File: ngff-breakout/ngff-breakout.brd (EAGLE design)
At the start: 90 x 80 mm, 77 parts, among them U2 LD1085D2T33R, X1 PINHD-2X4, X7 694108106102, X9 ZX360D-B-10P(30), Y4 MHF4, Y5 MHF4, Y6 MHF4

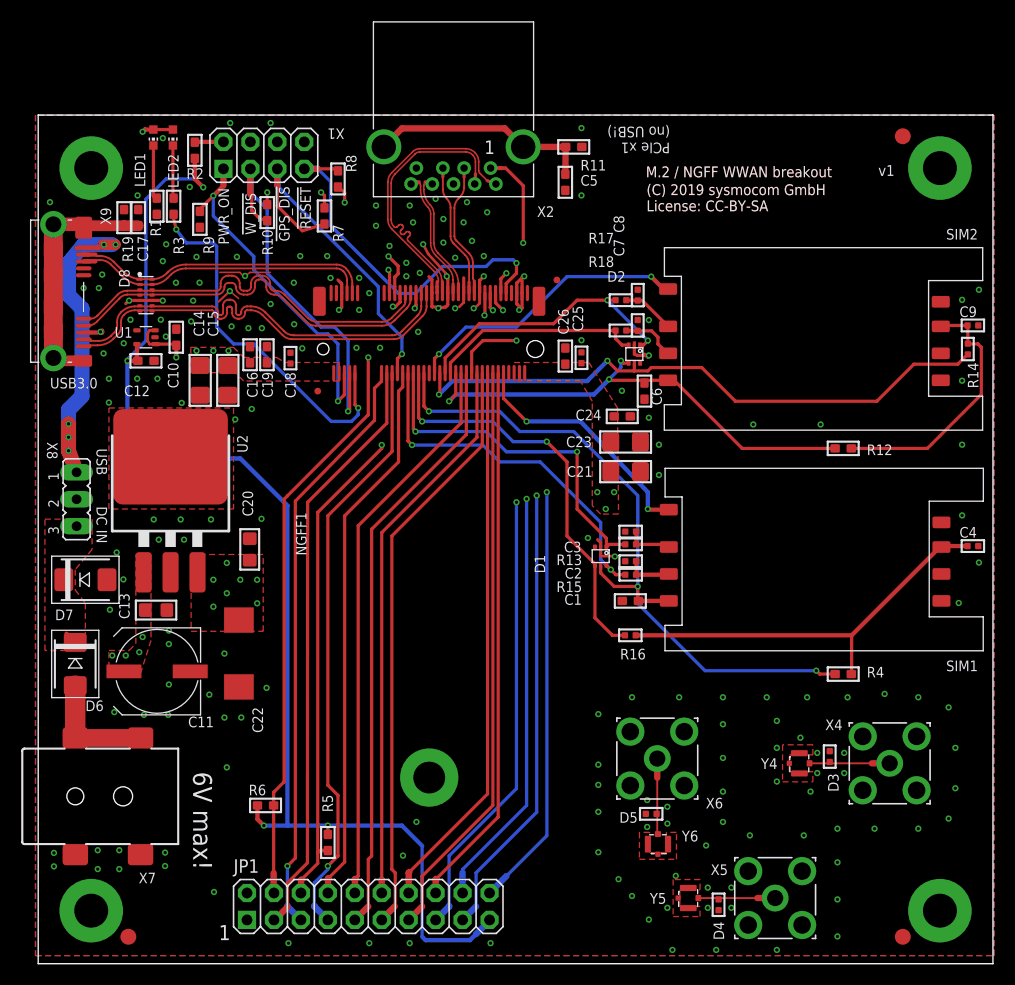
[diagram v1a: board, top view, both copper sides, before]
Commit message: ngff: move PCIe header 3mm inwards (solves OS#4210)
... and started OS#4211.
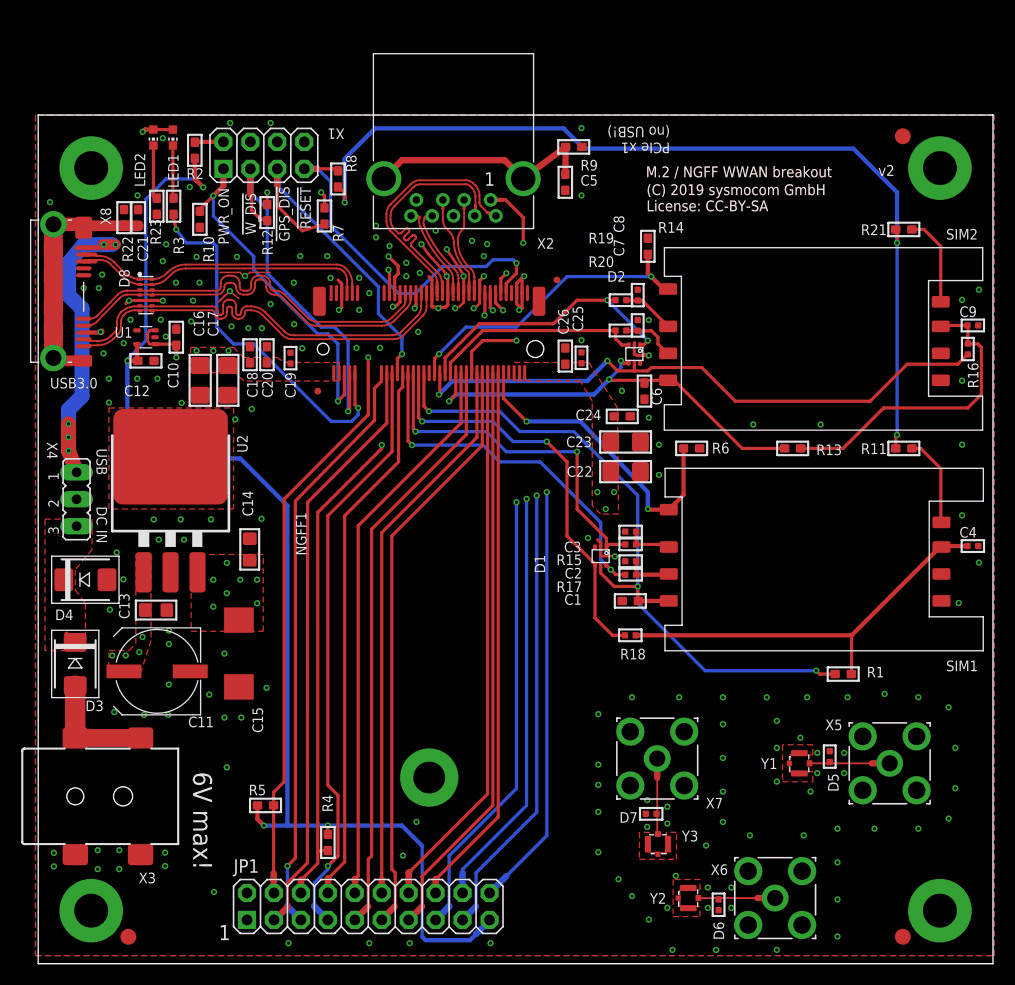
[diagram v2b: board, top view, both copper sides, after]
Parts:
- removed X9: ZX360D-B-10P(30), USB30-MICROB:ZX360D-B
- added R20: 47, rc-sysmocom:_0402
- added R21: 4.7k, rc-sysmocom:_0603
- added R22, R23: 330, rc-sysmocom:_0603
- added X3: 694108106102, Wurth_Elektronik_Electromechanic_DC_Power_Jack_Connectors_rev15c:694108106102
- C1, C10, C12, C24, C26, C5, C6: device rc-sysmocom:_0603 -> rc-sysmocom:_0603@1
- C13: device rc-sysmocom:_0805 -> rc-sysmocom:_0805@1
- C14: value 100u -> 10u; device rc-sysmocom:1206 -> rc-sysmocom:_0805@1
- C15: value 100u -> DNP; device rc-sysmocom:1206 -> rcl:SMC_E
- C16, C17: value 100n -> 100u; device rc-sysmocom:_0603 -> rc-sysmocom:1206@1
- C18: value 33p -> 100n; device rc-sysmocom:_0402 -> rc-sysmocom:_0603@1
- C19: value 10p -> 33p; device rc-sysmocom:_0603 -> rc-sysmocom:_0402@1
- C2, C25, C3, C4, C7, C8, C9: device rc-sysmocom:_0402 -> rc-sysmocom:_0402@1
- C20: value 10u -> 10p; device rc-sysmocom:_0805 -> rc-sysmocom:_0603@1
- C21: value 100u -> 100n; device rc-sysmocom:1206 -> rc-sysmocom:_0603@1
- C22: value DNP -> 100u; device rcl:SMC_E -> rc-sysmocom:1206@1
- C23: device rc-sysmocom:1206 -> rc-sysmocom:1206@1
- D3: value GG040205170N2P -> SD2114S040S5R0; device diodes-sysmocom:_0402 -> diodes-sysmocom:SMBDIODE
- D4: value GG040205170N2P -> SMBJP6KE6.8A-TP; device diodes-sysmocom:_0402 -> diodes-sysmocom:SMBDIODE
- D6: value SD2114S040S5R0 -> GG040205170N2P; device diodes-sysmocom:SMBDIODE -> diodes-sysmocom:_0402
- D7: value SMBJP6KE6.8A-TP -> GG040205170N2P; device diodes-sysmocom:SMBDIODE -> diodes-sysmocom:_0402
- LED1: value GREEN -> YELLOW
- LED2: value YELLOW -> GREEN
- R1: value 330 -> DNP
- R10: value 10k -> 100k
- R11: value 330 -> 4.7k
- R12, R4: value DNP -> 10k
- R13: value 47 -> DNP; device rc-sysmocom:_0402 -> rc-sysmocom:_0603
- R14: value 47 -> 47k; device rc-sysmocom:_0402 -> rc-sysmocom:_0603
- R19: value 330 -> 47; device rc-sysmocom:_0603 -> rc-sysmocom:_0402
- R6: value 10k -> 47k
- R9: value 100k -> 330
- X4: device laforge:SMA-F-S-TH -> jumper:JP2
- X7: value 694108106102 -> (none); device Wurth_Elektronik_Electromechanic_DC_Power_Jack_Connectors_rev15c:694108106102 -> laforge:SMA-F-S-TH
- X8: value (none) -> ZX360D-B-10P(30); device jumper:JP2 -> USB30-MICROB:ZX360D-B
- moved X4 80.6 mm to (3.62, 43.8), turned to 270 degrees
- moved R1 78.3 mm to (75.9, 27.3), turned to 0 degrees
- moved D3 71.7 mm to (3.49, 28.3)
- moved D4 67.1 mm to (4.45, 36.2), turned to 0 degrees
- moved D6 64.8 mm to (64.1, 5.56), turned to 90 degrees
- moved X7 60.0 mm to (58.4, 19.3), turned to 180 degrees
- moved R12 58.7 mm to (21.6, 70.8), turned to 90 degrees
- moved D7 57.7 mm to (57.8, 14.1)
- moved R6 52.4 mm to (61.6, 48.6)
- moved C21 51.8 mm to (9.43, 70.3), turned to 270 degrees
- moved R4 51.1 mm to (27.3, 11.4), turned to 90 degrees
- moved R19 47.5 mm to (54.9, 62.5), turned to 0 degrees
- moved R11 42.1 mm to (81.6, 48.6), turned to 0 degrees
- moved R16 41.7 mm to (87.6, 57.9), turned to 90 degrees
- moved C22 40.3 mm to (55.4, 46.4), turned to 180 degrees
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- renumbered JP501 to JP2, JP502 to JP3, Y4 to Y1, Y5 to Y2, Y6 to Y3
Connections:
- new net N$11: R21.2, SIM2.82
- new net N$9: R11.2, SIM1.82
- net !BODY_SAR: now also R5.1; no longer R6.1
- net !USIM1_RESET: now also R17.2; no longer R15.2
- net !USIM2_RESET: now also R20.2; no longer R18.2
- net !WAKE_ON_WWAN: now also R4.1; no longer R5.1
- net !W_DISABLE: now also R12.1; no longer R10.1
- net GND: now also C15.-, C18.1, C20.2, C22.1, D4.A, D6.1, D7.1, R10.1, R14.1, R22.1, R23.1, R6.1, X3.2, X3.3, X7.G1, X7.G2, X7.G3, X7.G4, X8.5, X8.8; no longer C15.1, C18.2, C20.1, C22.-, D3.1, D4.1, D7.A, R1.1, R11.1, R19.1, SIM1.82, SIM2.82, X4.G1, X4.G2, X4.G3, X4.G4, X7.2, X7.3, X9.5, X9.8
- net LDO_IN: now also X4.2; no longer X8.2
- net N$1: now also LED2.C, R23.2; no longer LED1.C, R1.2
- net N$10: now also C21.2, R22.2, X8.S1, X8.S2, X8.S3, X8.S4, X8.S5, X8.S6, X8.S7, X8.S8; no longer C17.2, R19.2, X9.S1, X9.S2, X9.S3, X9.S4, X9.S5, X9.S6, X9.S7, X9.S8
- net N$12: now also D3.C, D4.C, X4.3; no longer D6.C, D7.C, X8.3
- net N$13: now also D5.2, X5.C; no longer D3.2, X4.C
- net N$14: now also D6.2, X6.C; no longer D4.2, X5.C
- net N$17: now also X8.4; no longer X9.4
- net N$2: now also LED1.C; no longer LED2.C
- net N$3: now also D3.A, X3.1, X3.1-1; no longer D6.A, X7.1, X7.1-1
- net N$4: now also R9.2; no longer R11.2
- net N$7: now also D7.2, X7.C; no longer D5.2, X6.C
- net PWR_ON: now also R10.2; no longer R9.2
- net SIM1_DET: now also R6.2
- net SIM2_DET: now also R14.2
- net USB3.0_RX_N: now also X8.9; no longer X9.9
- net USB3.0_RX_P: now also X8.10; no longer X9.10
- net USB3.0_TX_N: now also X8.6; no longer X9.6
- net USB3.0_TX_P: now also X8.7; no longer X9.7
- net USB_VBUS: now also X4.1; no longer X9.1
- net USIM1_CLK: now also R15.2; no longer R13.2
- net USIM1_DATA: now also R1.2, R18.2; no longer R16.2, R4.2
- net USIM1_POWER: now also R1.1; no longer R4.1
- net USIM2_CLK: now also R19.2; no longer R17.2
- net USIM2_DATA: now also R13.2, R16.2; no longer R12.2, R14.2
- net USIM2_POWER: now also R13.1; no longer R12.1
- net VCC_1V8: now also R11.1, R12.2, R21.1, R4.2; no longer R10.2, R6.2
- net VCC_3V3: now also C15.+, C17.2, C18.2, C20.1, C22.2; no longer C15.2, C18.1, C20.2, C21.2, C22.+
- net _!USIM1_RESET: now also R17.1; no longer R15.1
- net _!USIM2_RESET: now also R20.1; no longer R18.1
- net _USB_D_N: now also X8.2; no longer X9.2
- net _USB_D_P: now also X8.3; no longer X9.3
- net _USIM1_CLK: now also R15.1; no longer R13.1
- net _USIM1_DATA: now also R18.1; no longer R16.1
- net _USIM2_CLK: now also R19.1; no longer R17.1
- net _USIM2_DATA: now also R16.1; no longer R14.1
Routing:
- net VCC_1V8: track 136.1 -> 221.5 mm, vias 7 -> 9
- net N$11: track 0.00 -> 8.62 mm
- net N$9: track 0.00 -> 8.61 mm
- net SIM1_DET: track 23.3 -> 29.7 mm
- net USIM2_POWER: track 46.3 -> 41.6 mm
- net USIM2_DATA: track 25.1 -> 29.8 mm
- net PCIE_TX_N: track 26.4 -> 23.1 mm
- net REFCLK_P: track 12.6 -> 9.27 mm
- net PCIE_RX_N: track 12.1 -> 8.81 mm
- net PCIE_RX_P: track 12.1 -> 8.79 mm
- net REFCLK_N: track 12.5 -> 9.38 mm
- net !WAKE: track 26.4 -> 23.4 mm
- net GND: track 49.8 -> 52.6 mm, vias 193 -> 188
- net SIM2_DET: track 27.1 -> 29.3 mm
- net PCIE_TX_P: track 25.7 -> 24.0 mm
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
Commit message: ngff: remove bogus packages names with '@1' by re-importing std lib
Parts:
- C1, C10, C12, C18, C20, C21, C24, C26, C5, C6: device rc-sysmocom:_0603@1 -> rc-sysmocom:_0603
- C13, C14: device rc-sysmocom:_0805@1 -> rc-sysmocom:_0805
- C16, C17, C22, C23: device rc-sysmocom:1206@1 -> rc-sysmocom:1206
- C19, C2, C25, C3, C4, C7, C8, C9: device rc-sysmocom:_0402@1 -> rc-sysmocom:_0402

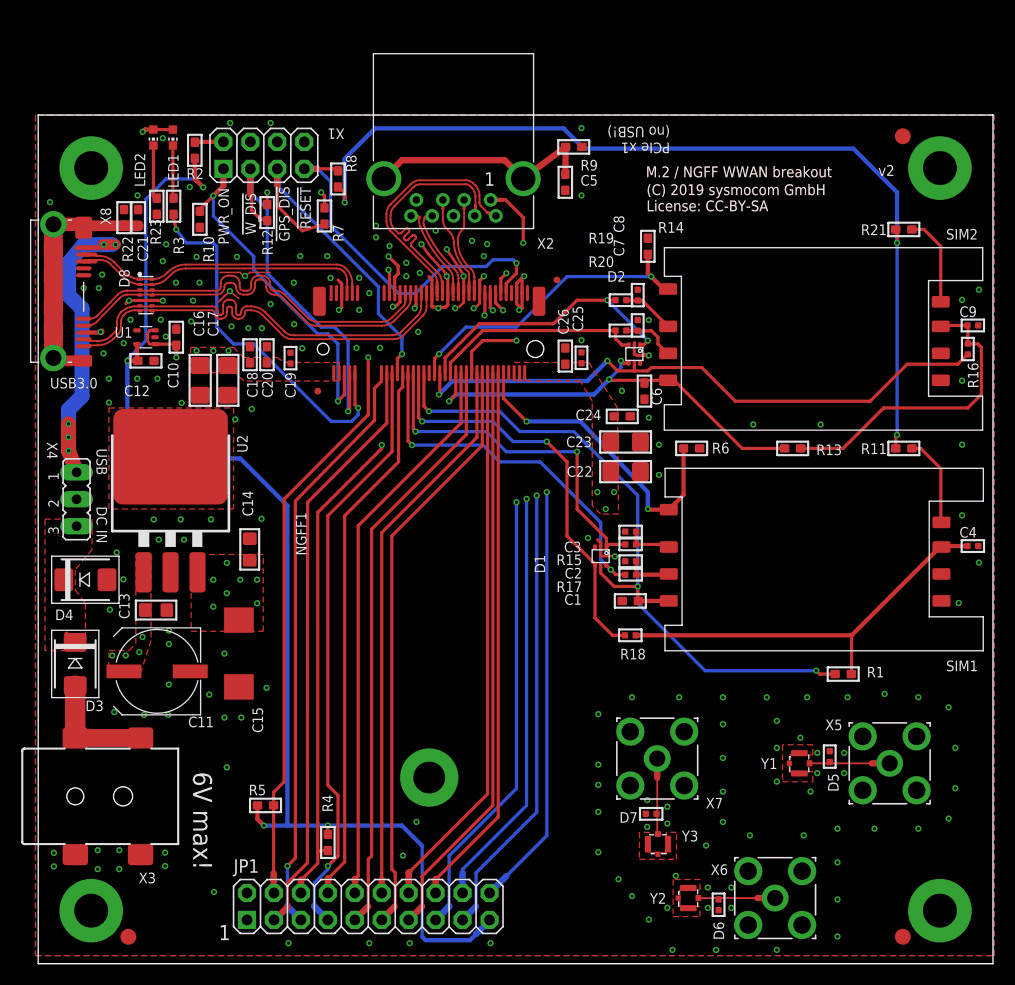
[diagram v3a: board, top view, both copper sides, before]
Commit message: ngff: make room for 2x5 header and route SIM2 signals there
adresses OS#4211
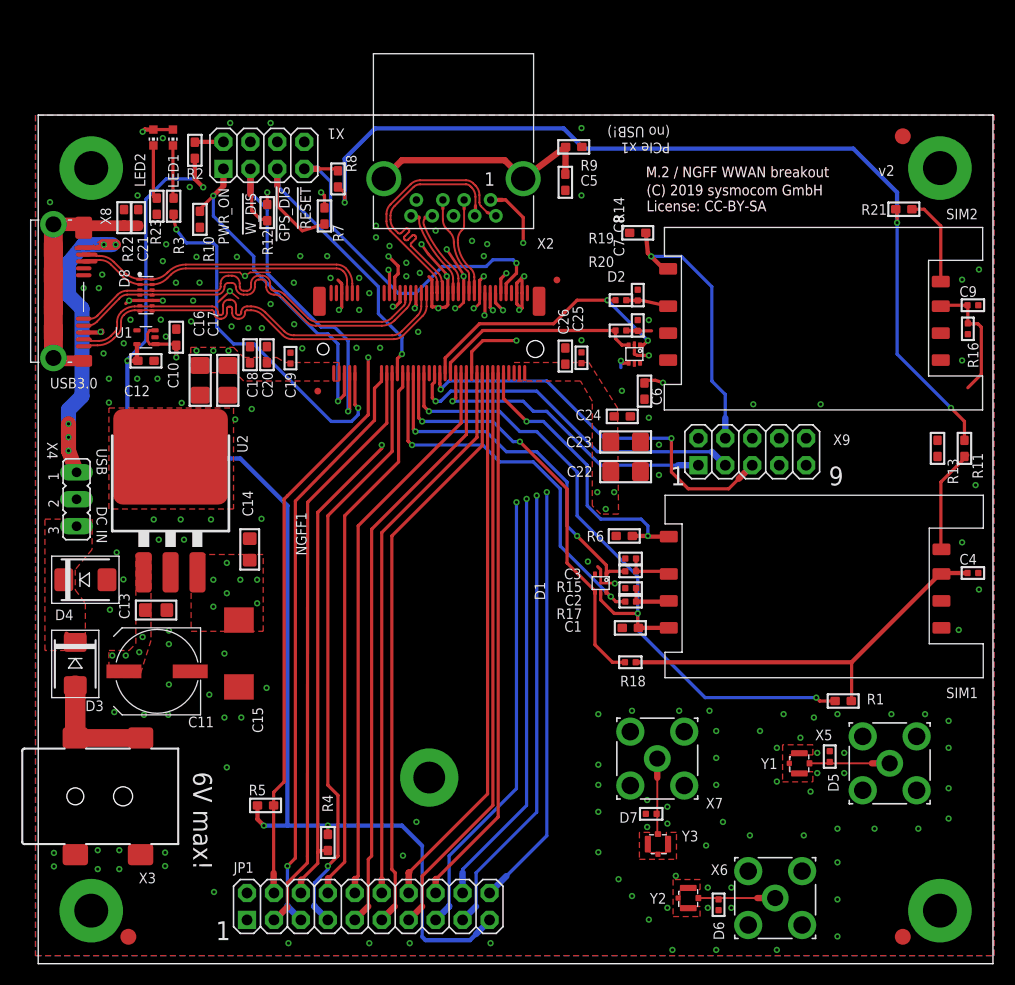
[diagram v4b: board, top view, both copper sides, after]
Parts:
- added X9: (no value), laforge:2X05
- moved R13 13.7 mm to (84.8, 48.6), turned to 90 degrees
- moved R6 10.4 mm to (55.2, 40.3), turned to 0 degrees
- moved R11 5.72 mm to (87.3, 48.6), turned to 270 degrees
- moved R15 2.54 mm to (55.8, 37.0)
- moved C1 2.54 mm to (55.8, 31.7)
- moved C2 2.54 mm to (55.8, 35.4)
- moved C3 2.54 mm to (55.8, 38.2)
- moved C4 2.54 mm to (88.1, 36.8)
- moved D1 2.54 mm to (53.0, 35.9)
- moved R1 2.54 mm to (75.9, 24.8)
- moved R17 2.54 mm to (55.8, 34.1)
- moved R18 2.54 mm to (55.8, 28.4)
- moved SIM1 2.54 mm to (72.3, 35.6)
- moved C9 1.91 mm to (88.1, 62.1)
- moved R16 1.91 mm to (87.6, 59.8)
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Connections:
- new net N$15: R16.1, X9.6
- new net N$20: X9.7
- new net N$21: X9.9
- new net N$22: X9.10
- new net N$23: X9.8
- new net _SIM2_DET: NGFF1.40, X9.3
- new net _USIM2_POWER: NGFF1.48, X9.1
- net SIM2_DET: now also X9.4; no longer NGFF1.40
- net USIM2_DATA: now also D2.5
- net USIM2_POWER: now also X9.2; no longer NGFF1.48
- net _USIM2_DATA: now also X9.5; no longer D2.5, R16.1
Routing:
- net USIM2_POWER: track 41.6 -> 3.50 mm, vias 3 -> 2
- net _SIM2_DET: track 0.00 -> 33.5 mm, vias 0 -> 1
- net _USIM2_POWER: track 0.00 -> 28.4 mm, vias 0 -> 1
- net _USIM2_DATA: track 57.6 -> 38.2 mm
- net USIM2_DATA: track 29.8 -> 12.5 mm
- net SIM2_DET: track 29.3 -> 26.2 mm, vias 2 -> 1
- net !USIM2_RESET: track 5.49 -> 2.97 mm
- net _!USIM1_RESET: track 34.7 -> 36.9 mm
- net SIM1_DET: track 29.7 -> 27.6 mm
- net VCC_1V8: track 221.5 -> 223.3 mm
- net N$9: track 8.61 -> 9.96 mm
- net _USIM1_DATA: track 39.2 -> 40.3 mm
- net USIM2_CLK: track 5.22 -> 4.27 mm
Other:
- board text added: "9"

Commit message: ngff: 2/2 make room for 2x5 header and route SIM2 signals there
...and run ERC/DRC

adresses OS#4211
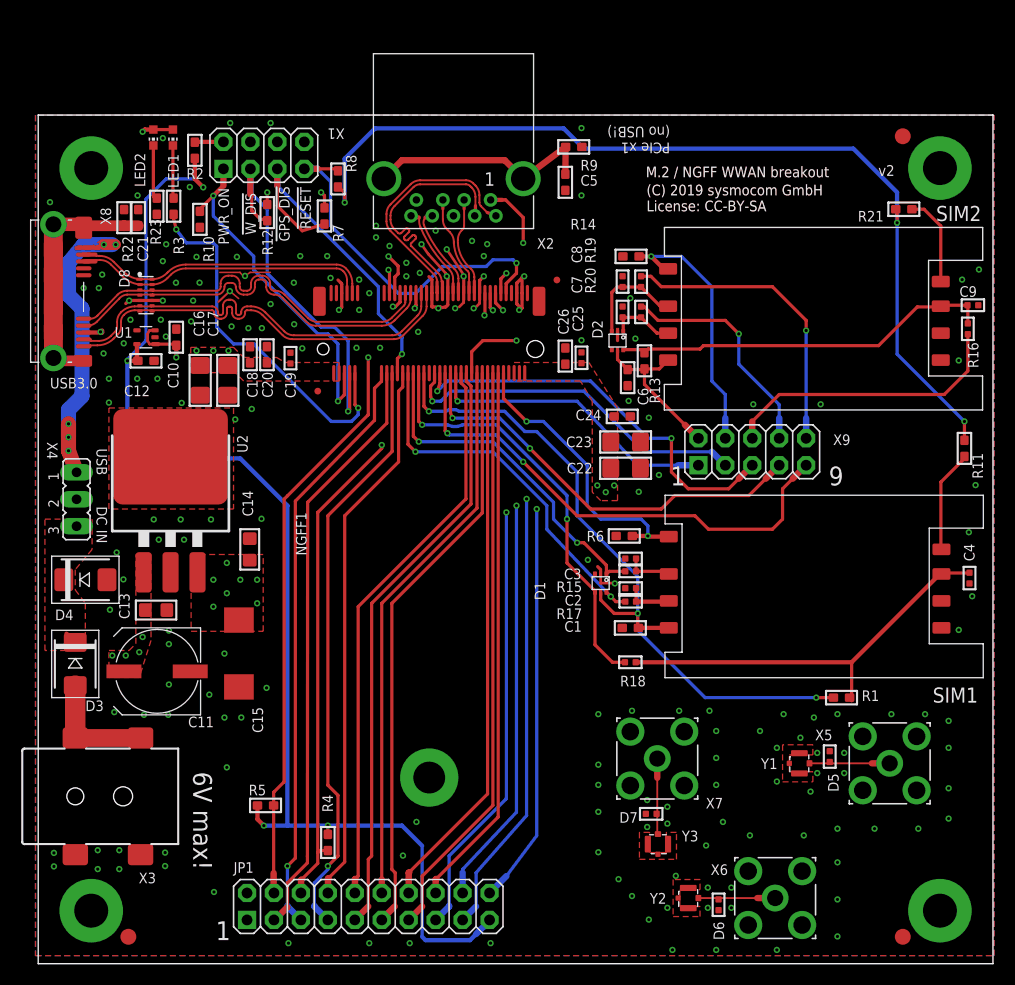
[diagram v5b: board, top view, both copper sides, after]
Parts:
- moved R13 28.8 mm to (57.1, 56.8)
- moved R19 2.58 mm to (56.8, 64.3), turned to 270 degrees
- moved R20 2.58 mm to (56.8, 61.4), turned to 270 degrees
- moved R14 2.31 mm to (55.9, 66.7)
- moved C6 2.03 mm to (55.6, 55.2)
- moved D2 2.03 mm to (54.6, 58.7)
- moved C7 1.91 mm to (55.1, 61.4)
- moved C8 1.91 mm to (55.1, 64.3)
- moved C4 0.57 mm to (87.8, 36.4), turned to 270 degrees
- moved R1 0.35 mm to (75.7, 25.1)
- moved C22 0.32 mm to (55.4, 46.7)
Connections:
- removed net N$20: X9.7
- removed net N$21: X9.9
- removed net N$22: X9.10
- removed net N$23: X9.8
- new net N$16: R20.1, X9.8
- new net N$19: R19.1, X9.10
- net !USIM2_RESET: now also D2.1
- net USIM2_CLK: now also D2.3
- net USIM2_DATA: now also D2.6; no longer D2.5
- net USIM2_POWER: now also D2.5; no longer D2.4
- net _!USIM2_RESET: now also X9.7; no longer D2.3, R20.1
- net _USIM2_CLK: now also X9.9; no longer D2.1, R19.1
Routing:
- net N$19: track 0.00 -> 28.4 mm, vias 0 -> 1
- net N$15: track 0.00 -> 27.3 mm
- net USIM2_DATA: track 12.5 -> 36.9 mm
- net N$16: track 0.00 -> 21.7 mm, vias 0 -> 1
- net _USIM2_CLK: track 26.0 -> 47.5 mm
- net _!USIM2_RESET: track 20.0 -> 40.3 mm, vias 0 -> 2
- net USIM2_POWER: track 3.50 -> 15.1 mm, vias 2 -> 0
- net USIM2_CLK: track 4.27 -> 10.2 mm
- net !USIM2_RESET: track 2.97 -> 6.86 mm
- net _!USIM1_RESET: track 36.9 -> 35.3 mm
- net GND: track 52.1 -> 50.8 mm
- net SIM2_DET: track 26.2 -> 24.9 mm
- net _USIM1_CLK: track 33.9 -> 32.8 mm
- net ANTCTL3: track 64.7 -> 63.7 mm
- net ANTCTL2: track 63.9 -> 62.9 mm
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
